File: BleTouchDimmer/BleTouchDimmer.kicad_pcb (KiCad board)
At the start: 2 copper layers, 113 x 56.1 mm, 68 parts, among them J1 Conn_01x03, J2 Conn_01x03, J3 JTAG, J4 Conn_01x06, J5 SLIDER1, J6 SLIDER2, P3 POWER, Q1 PDTC123J, Q2 PDTC123J, Q3 PDTC123J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

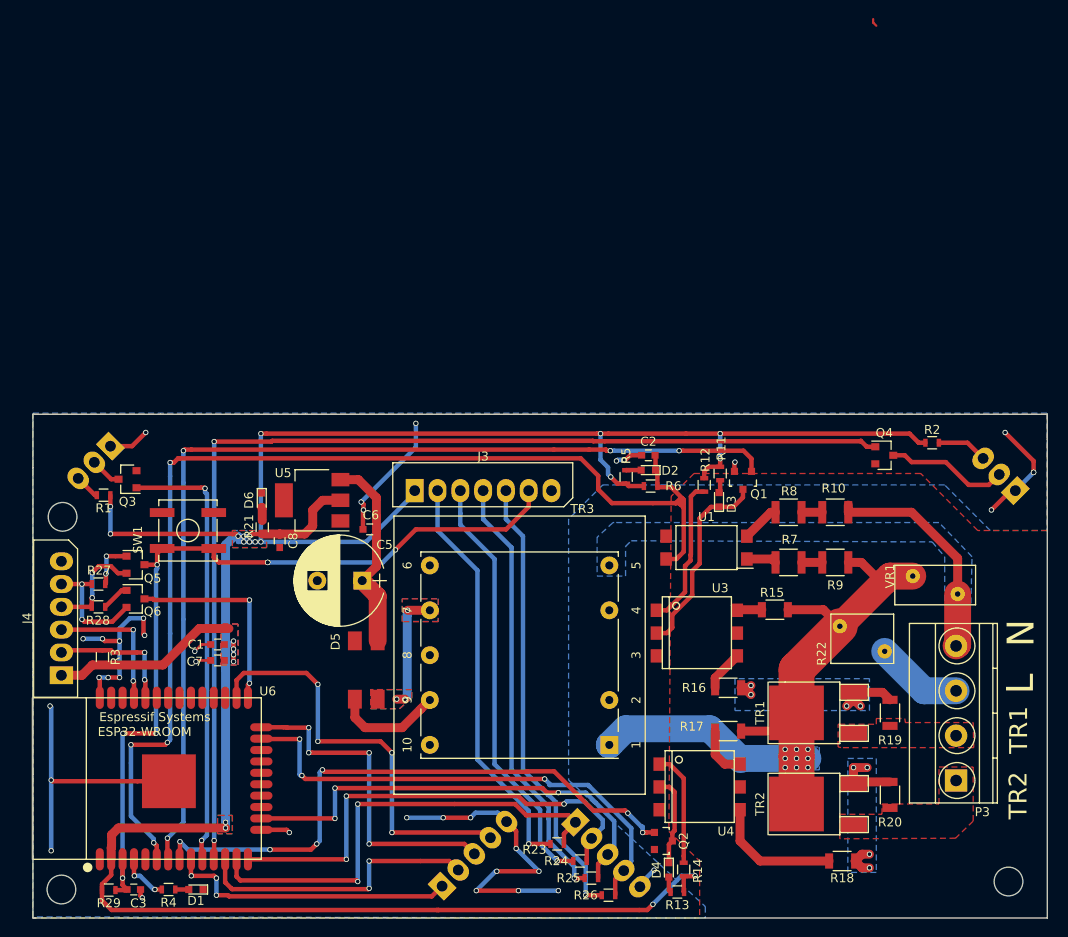
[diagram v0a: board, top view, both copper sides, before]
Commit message: Spreaded pcb wires to get less crosstalk.
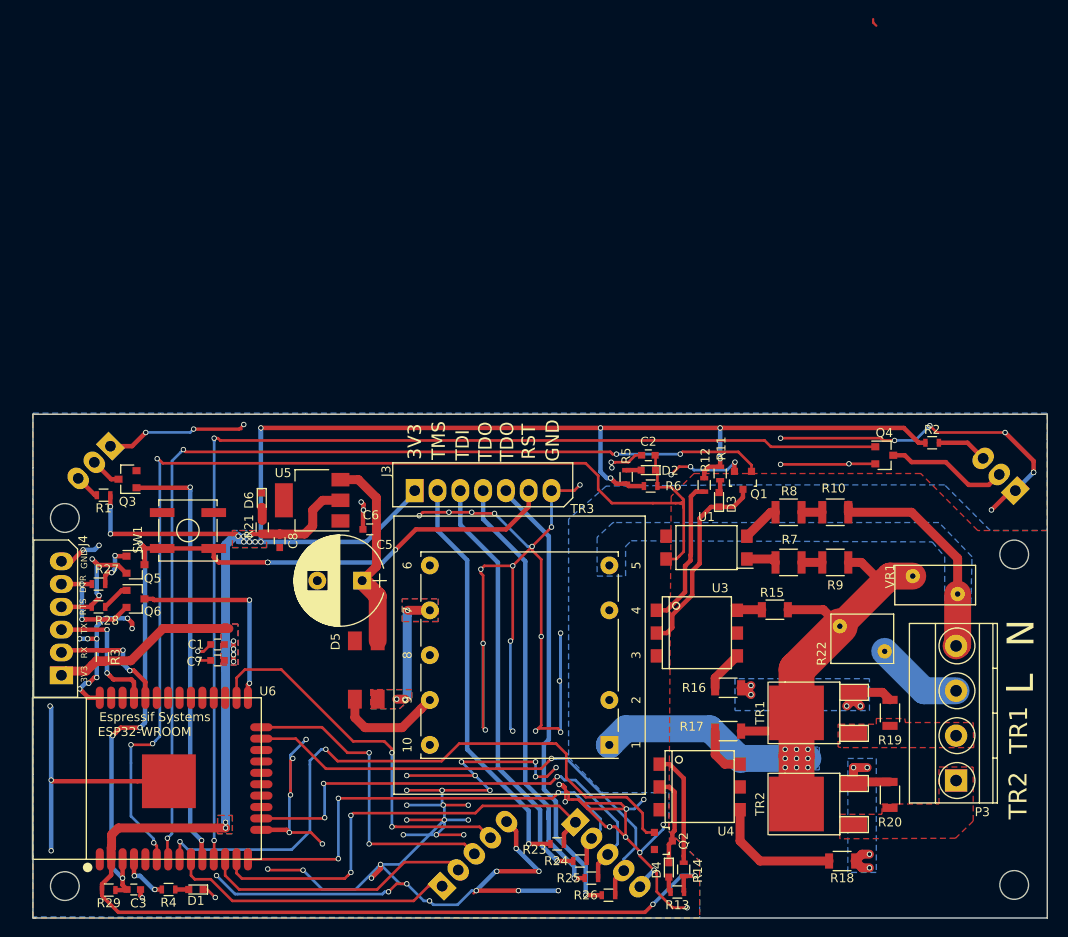
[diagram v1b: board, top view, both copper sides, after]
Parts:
- added REF**: MountingHole_3.2mm_M3, Mounting_Holes:MountingHole_3.2mm_M3, F.Cu at (213.5, 78.9)
- moved REF** 0.74 mm to (213.5, 115.7)
- moved REF** 0.54 mm to (107.7, 115.8)
- moved REF** 0.28 mm to (107.7, 74.8)
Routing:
- net GND: track 130.6 -> 480.0 mm, vias 36 -> 101
- net /TR2_CTRL: track 66.7 -> 72.9 mm, vias 6 -> 2
- net /RESET: track 93.5 -> 97.2 mm
- net +3V3: track 309.6 -> 313.0 mm
- net /TOUCH0: track 47.4 -> 44.0 mm, vias 4 -> 2
- net /TOUCH7: track 32.3 -> 30.0 mm, vias 2 -> 0
- net /RTS: track 11.7 -> 13.9 mm
- net /TOUCH6/MTMS: track 52.3 -> 50.3 mm
- net /TOUCH4/MTCK: track 51.3 -> 53.3 mm
- net /TOUCH2: track 37.2 -> 35.5 mm, vias 4 -> 2
- net /LED1: track 49.4 -> 48.1 mm
- net /RX: track 15.6 -> 14.6 mm
- net /LED2: track 120.6 -> 121.4 mm
- net /TOUCH8: track 32.3 -> 31.6 mm, vias 3 -> 0
- net /TOUCH3/MTDO: track 55.9 -> 55.3 mm, vias 3 -> 1
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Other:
- board text added: "3V3"
- board text added: "DTR"
- board text added: "RST"
- board text added: "RTS"
- board text added: "RX"
- board text added: "TDI"
- board text added: "TDO"
- board text added: "TMS"
- board text added: "TX"

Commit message: Made small changes and generated gerbers.
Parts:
- moved REF** 0.68 mm to (108.0, 75.4)
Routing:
- net GND: track 480.0 -> 501.6 mm, vias 101 -> 108
- net (no net): track 0.89 -> 2.63 mm
- net Net-(J3-Pad3): track 47.5 -> 48.6 mm
- net /TOUCH2: track 35.5 -> 34.6 mm
- net Net-(J3-Pad2): track 46.0 -> 46.8 mm
- net Net-(J3-Pad4): track 49.4 -> 48.7 mm
- net /TOUCH3/MTDO: track 55.3 -> 55.9 mm
- net /TOUCH4/MTCK: track 53.3 -> 52.6 mm
- net /TOUCH6/MTMS: track 50.3 -> 49.8 mm
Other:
- outline, holes or cut-outs redrawn
- board text added: "BleTouchDimmer V1 Egert 2017"

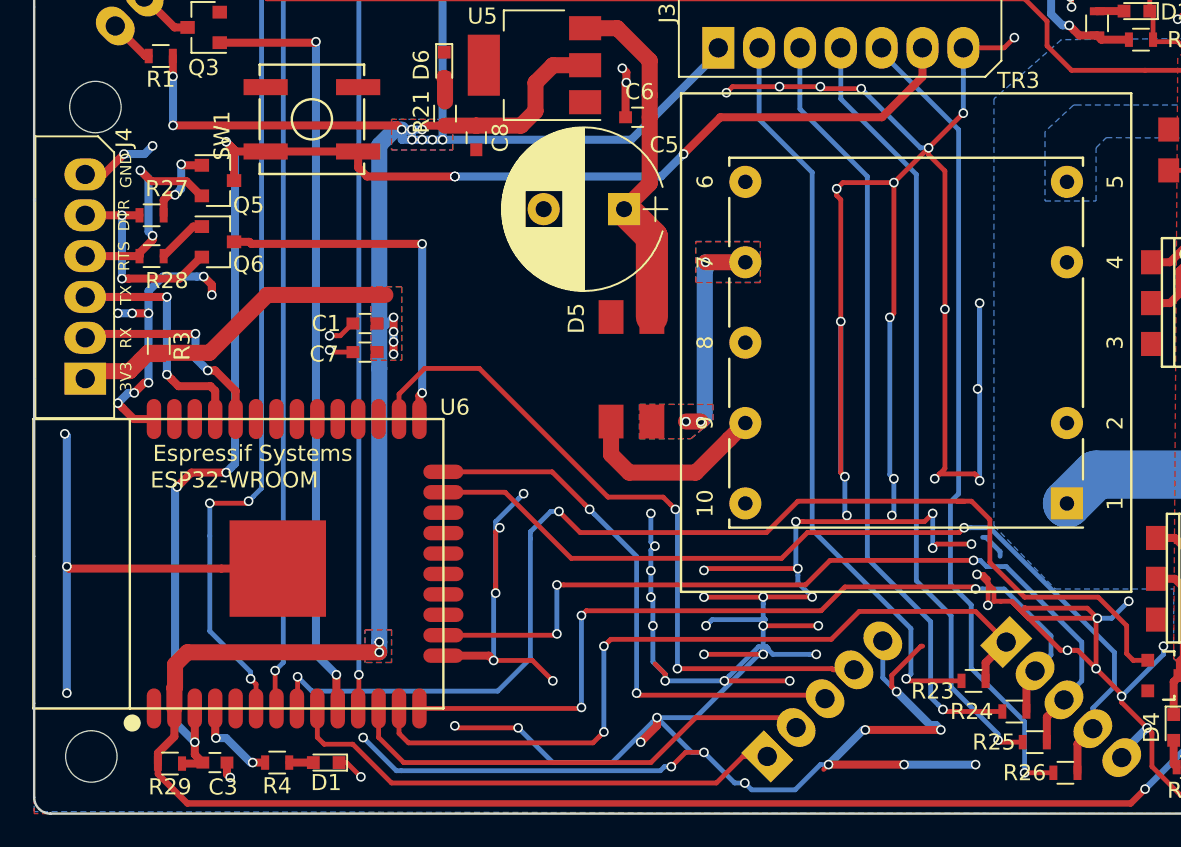
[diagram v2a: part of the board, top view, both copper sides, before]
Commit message: New gerbers and ordered pcbs.
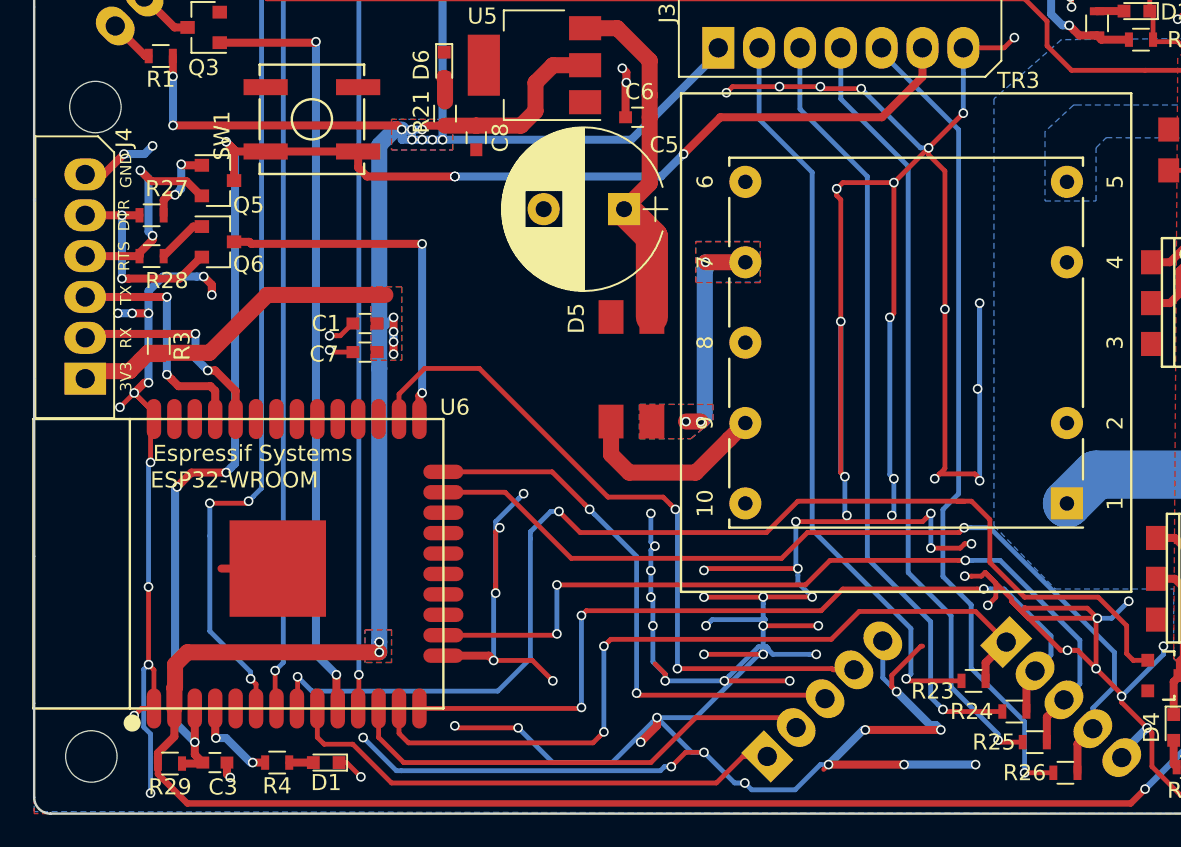
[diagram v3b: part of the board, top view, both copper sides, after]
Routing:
- net GND: track 501.6 -> 505.7 mm, vias 108 -> 110
- net (no net): track 2.63 -> 0.89 mm
